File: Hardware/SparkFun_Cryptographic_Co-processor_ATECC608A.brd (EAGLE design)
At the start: 25.4 x 25.4 mm, 41 parts, among them J1 QWIIC, J2 QWIIC, J3 PTH, U1 ATECC608A

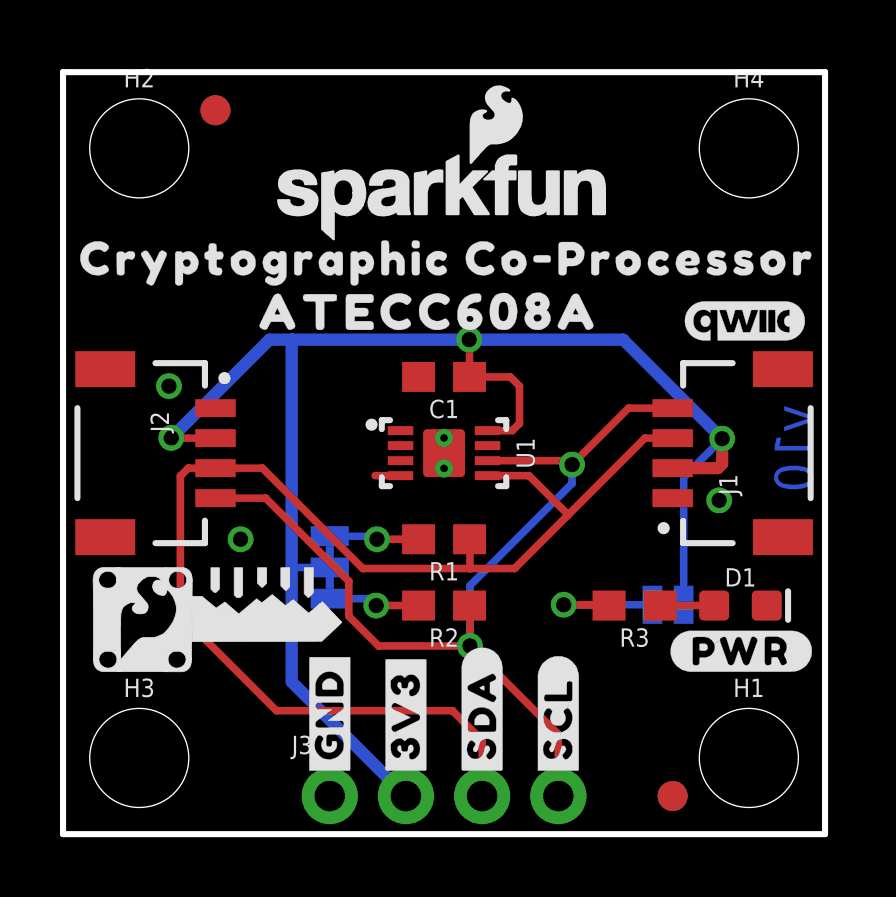
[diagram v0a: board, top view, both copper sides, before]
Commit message: Move to dual-type package (UDFN and SOIC)
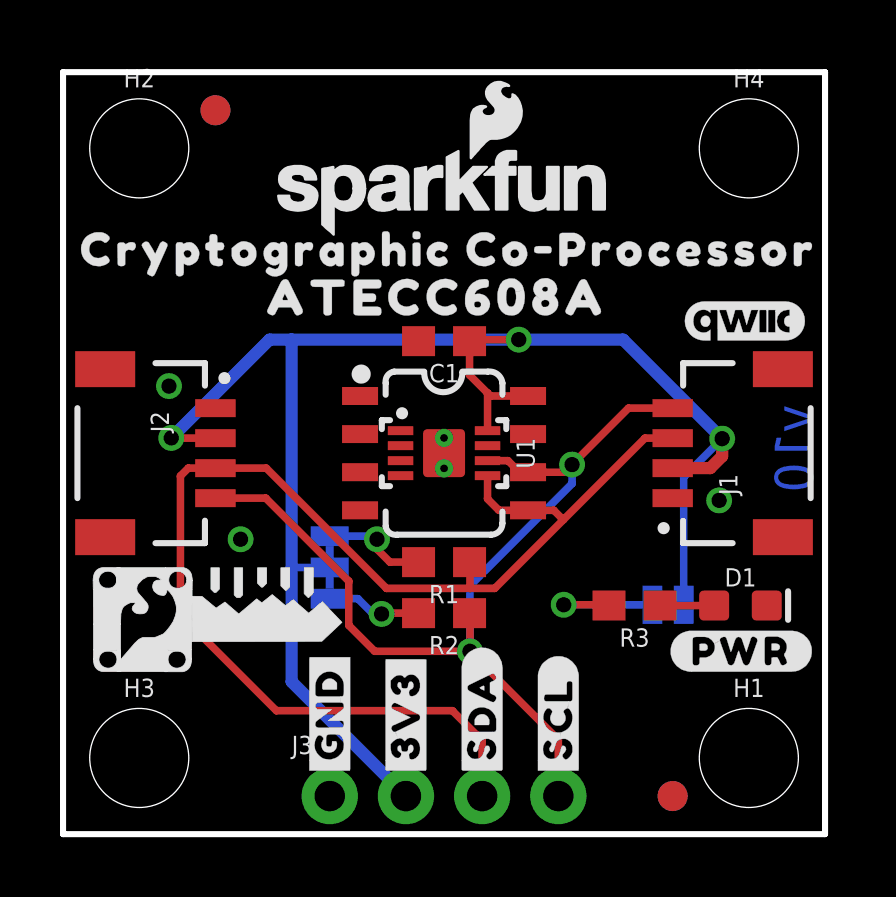
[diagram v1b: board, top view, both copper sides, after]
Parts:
- U1: device SparkFun-IC-Special-Function:UDFN_2X3MM -> SparkFun-IC-Special-Function:DUAL_UDFN_2X3MM_SOIC-8
- moved C1 1.19 mm to (12.7, 16.4)
- moved R1 0.76 mm to (12.7, 9.07)
- moved U$5 0.55 mm to (12.5, 17.9)
- moved U$7 0.55 mm to (12.3, 17.9)
- moved U$19 0.31 mm to (12.7, 19.5)
- moved U$9 0.31 mm to (12.9, 19.5)
- moved R2 0.25 mm to (12.7, 7.37)
- moved LOGO1 0.15 mm to (12.7, 21.4)
- moved LOGO2 0.15 mm to (12.7, 21.4)
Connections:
- net 3.3V: now also U1.8S
- net GND: now also U1.4S
- net SCL: now also U1.6S
- net SDA: now also U1.5S
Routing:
- net GND: track 0.85 -> 0.00 mm
- net SDA: track 42.2 -> 43.0 mm
- net 3.3V: track 54.7 -> 55.4 mm
- net N$4: track 3.00 -> 3.51 mm
